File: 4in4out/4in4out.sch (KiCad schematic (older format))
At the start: 60 parts

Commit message: Suppression des PNP
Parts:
- removed D? (x4): LED, symbol LED
- removed D? (x3): DIODE, symbol DIODE
- removed K? (x3): G5T-1-12VDC, symbol G5T-1-12VDC
- removed P? (x3): CONN_2, symbol CONN_2
- removed Q? (x4): PNP, symbol PNP
- removed Q? (x3): NPN, symbol NPN
- removed R? (x12): R, symbol R
- added D? (x4): LED, symbol LED
- added D? (x3): DIODE, symbol DIODE
- added K? (x3): G5T-1-12VDC, symbol G5T-1-12VDC
- added P? (x3): CONN_2, symbol CONN_2
- added Q? (x3): NPN, symbol NPN
- added R? (x8): R, symbol R
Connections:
- wire segments 125 -> 113
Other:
- moved on the sheet: D?, K?, P?, Q?

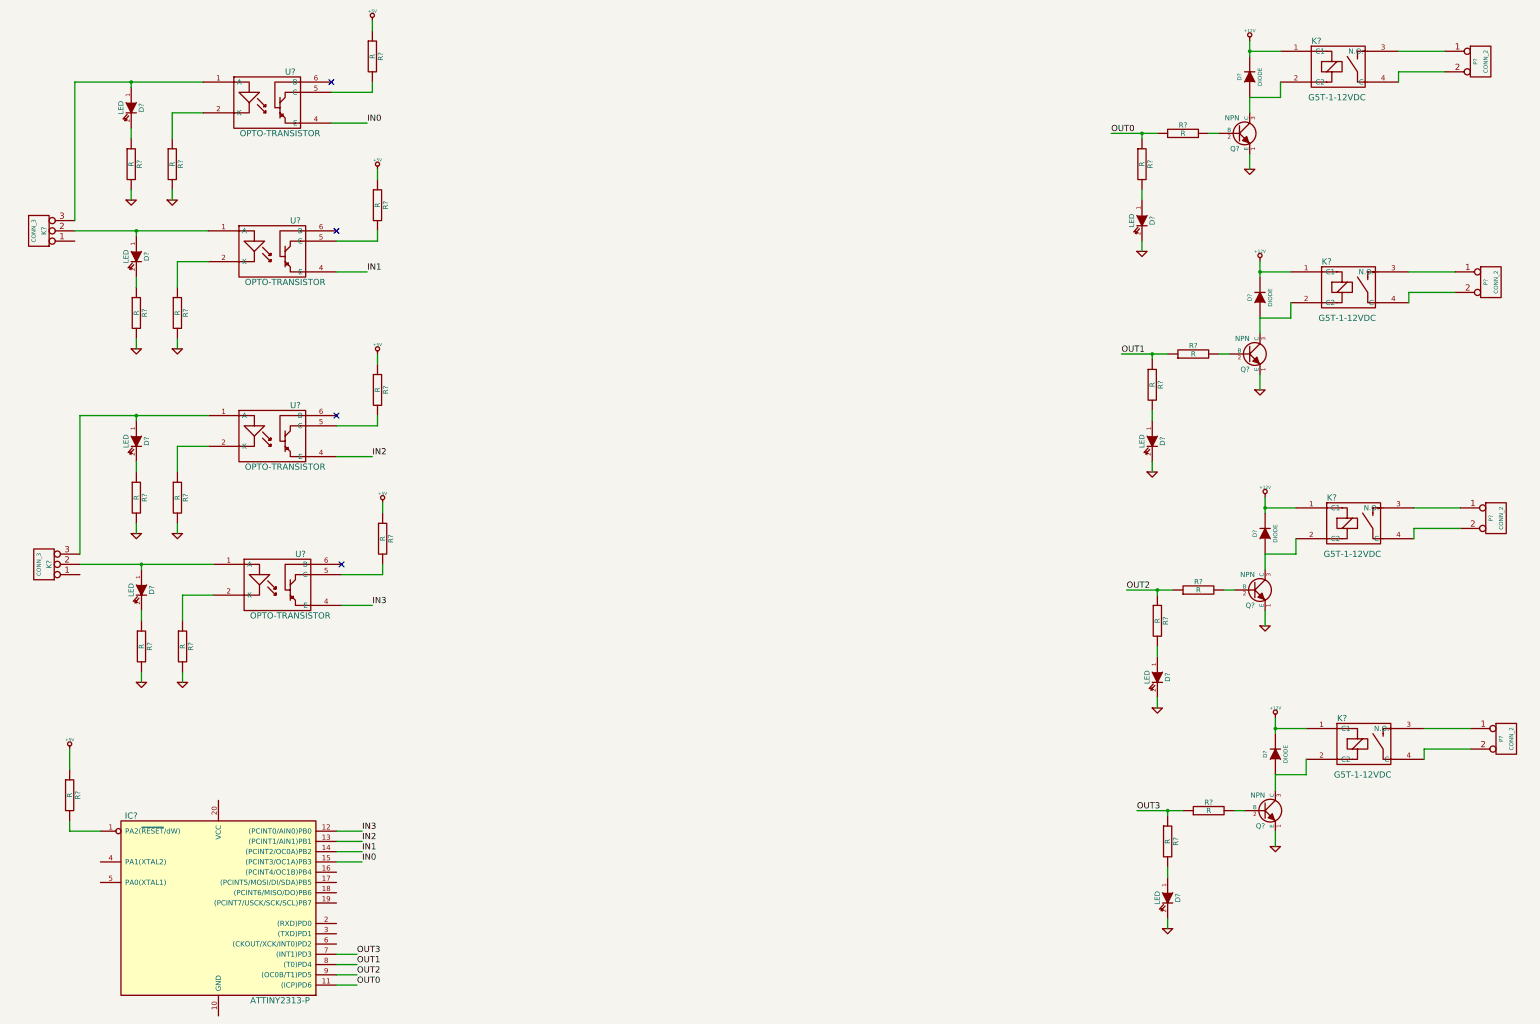
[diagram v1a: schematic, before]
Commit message: Mise ? jour de la carte 4in4out : Ajout des connecteurs et nommage des composants
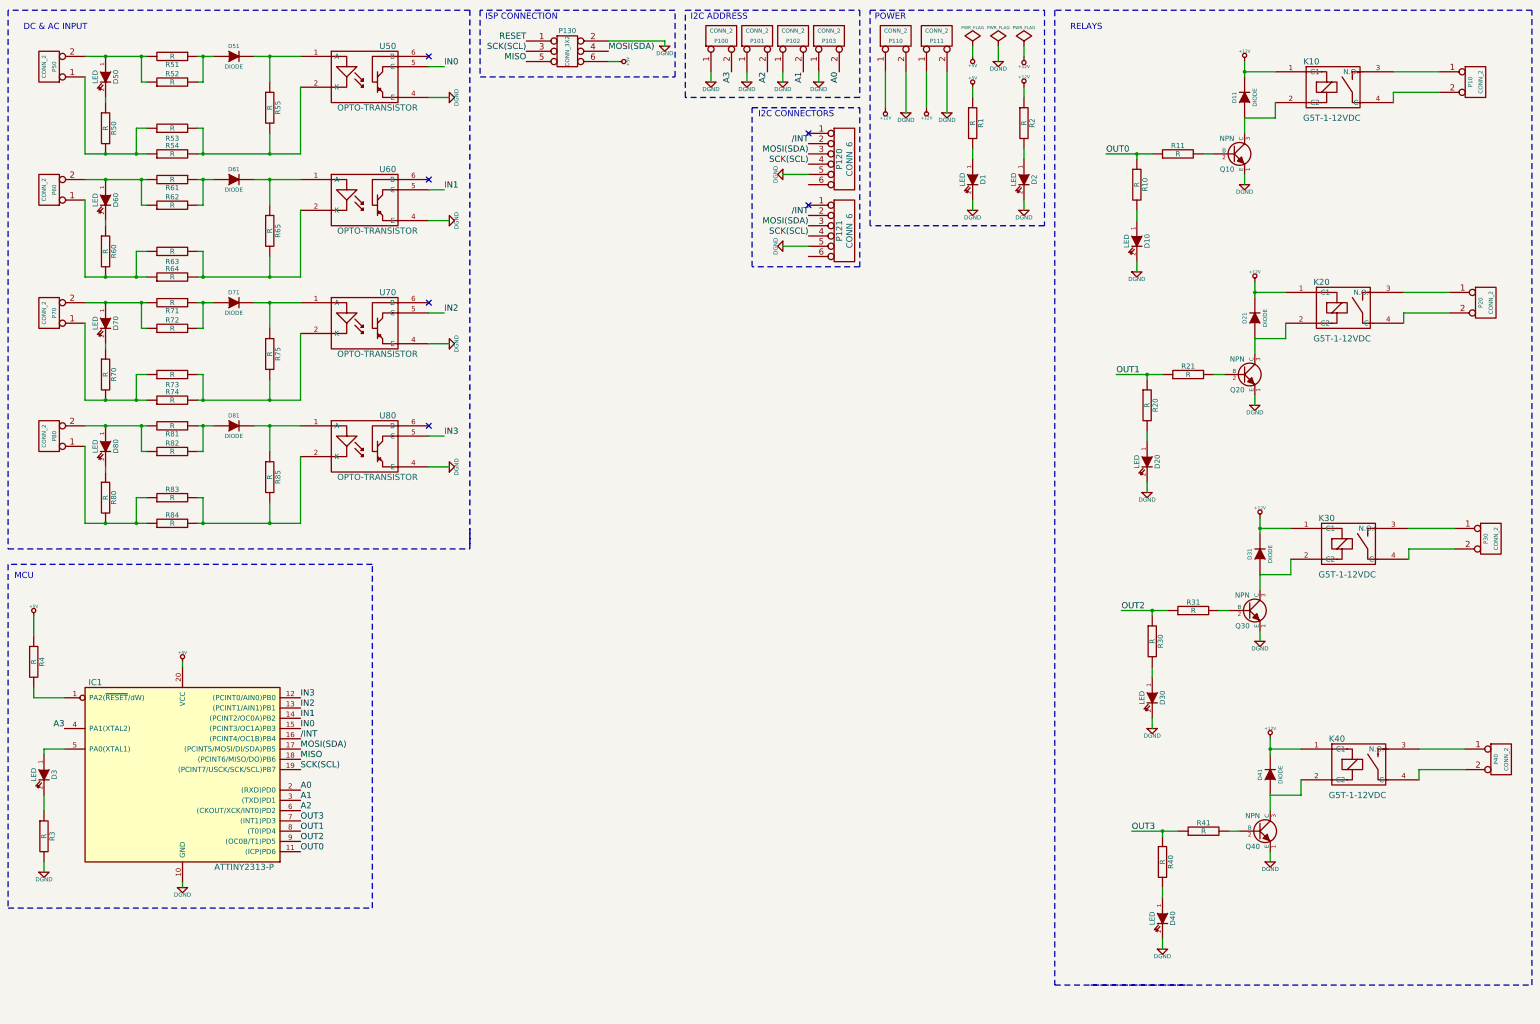
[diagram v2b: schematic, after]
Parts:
- removed D? (x4): LED, symbol LED
- removed K? (x2): CONN_3, symbol CONN_3
- removed R? (x12): R, symbol R
- removed U? (x3): OPTO-TRANSISTOR, symbol OPTO-TRANSISTOR
- added D1, D2, D3, D50, D60, D70, D80: LED, symbol LED
- added D51, D61, D71, D81: DIODE, symbol DIODE
- added P100, P101, P102, P103, P110, P111, P50, P60, P70, P80: CONN_2, symbol CONN_2
- added P120, P121: CONN_6, symbol CONN_6
- added P130: CONN_3X2, symbol CONN_3X2
- added R1, R2, R3, R50, R51, R52, R53, R54, R55, R60, R61, R62, R63, R64, R65, R70, R71, R72, R73, R74, R75, R80, R81, R82, R83, R84, R85: R, symbol R
- added U60, U70, U80: OPTO-TRANSISTOR, symbol OPTO-TRANSISTOR
- gave numbers to parts that had none: 31
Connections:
- net GND is gone; now on net DGND: D10.2 (K), D20.2 (K), D30.2 (K), D40.2 (K), Q10.1 (E), Q20.1 (E), Q30.1 (E), Q40.1 (E)
- net +12V: now also P110.1 (P1), P111.1 (P1), R2.1
- net +5V: now also IC1.20 (VCC), P130.6, R1.1
- net IN0: now also U50.5 (C); no longer U50.4 (E)
- net IN1: now also U60.5 (C)
- net IN2: now also U70.5 (C)
- net IN3: now also U80.5 (C)
- net DGND: now reaches IC1.10 (GND)
- net DGND: now also U50.4 (E), D1.2 (K), D2.2 (K), P100.1 (P1), P101.1 (P1), P102.1 (P1), P103.1 (P1), P110.2 (PM), P111.2 (PM), P120.5, P121.5, P130.2, R3.2, U60.4 (E), U70.4 (E), U80.4 (E)
- net /INT: now reaches IC1.16 ((PCINT4/OC1B)PB4)
- net /INT: now also P120.2, P121.2
- net MOSI(SDA): now reaches IC1.17 ((PCINT5/MOSI/DI/SDA)PB5)
- net MOSI(SDA): now also P120.3, P121.3, P130.4
- net MISO: now reaches IC1.18 ((PCINT6/MISO/DO)PB6)
- net MISO: now also P130.5
- net SCK(SCL): now reaches IC1.19 ((PCINT7/USCK/SCK/SCL)PB7)
- net SCK(SCL): now also P120.4, P121.4, P130.3
- net A0: now reaches IC1.2 ((RXD)PD0)
- net A0: now also P103.2 (PM)
- net A1: now reaches IC1.3 ((TXD)PD1)
- net A1: now also P102.2 (PM)
- net A3: now reaches IC1.4 (PA1(XTAL2))
- net A3: now also P100.2 (PM)
- net at IC1.5 (PA0(XTAL1)): now also D3.1 (A)
- net A2: now reaches IC1.6 ((CKOUT/XCK/INT0)PD2)
- net A2: now also P101.2 (PM)
- net at U50.1 (A): now also D51.2 (K), R55.1
- net at U50.2 (K): now also R53.2, R54.2, R55.2
- new net: D51.1 (A), R51.1, R52.2
- new net: D50.1 (A), P50.2 (PM), R51.2, R52.1
- new net: P50.1 (P1), R50.2, R53.1, R54.1
- new net: D50.2 (K), R50.1
- new net: D61.2 (K), R65.1, U60.1 (A)
- new net: R63.2, R64.2, R65.2, U60.2 (K)
- new net: D61.1 (A), R61.1, R62.2
- new net: D60.1 (A), P60.2 (PM), R61.2, R62.1
- new net: P60.1 (P1), R60.2, R63.1, R64.1
- new net: D60.2 (K), R60.1
- new net: D71.2 (K), R75.1, U70.1 (A)
- new net: R73.2, R74.2, R75.2, U70.2 (K)
- new net: D71.1 (A), R71.1, R72.2
- new net: D70.1 (A), P70.2 (PM), R71.2, R72.1
- new net: P70.1 (P1), R70.2, R73.1, R74.1
- new net: D70.2 (K), R70.1
- new net: D81.2 (K), R85.1, U80.1 (A)
- new net: R83.2, R84.2, R85.2, U80.2 (K)
- new net: D81.1 (A), R81.1, R82.2
- new net: D80.1 (A), P80.2 (PM), R81.2, R82.1
- new net: P80.1 (P1), R80.2, R83.1, R84.1
- new net: D80.2 (K), R80.1
- new net: D3.2 (K), R3.1
- new net: D2.1 (A), R2.2
- new net: D1.1 (A), R1.2
- new net RESET: P130.1
- no-connect marks 4 -> 6
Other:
- note added: "DC & AC INPUT"
- note added: "I2C ADDRESS"
- note added: "I2C CONNECTORS"
- note added: "ISP CONNECTION"
- note added: "MCU"
- note added: "POWER"
- note added: "RELAYS"
- moved on the sheet: D10, D11, D20, D21, D30, D31, D40, D41, IC1, K10, K20, K30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

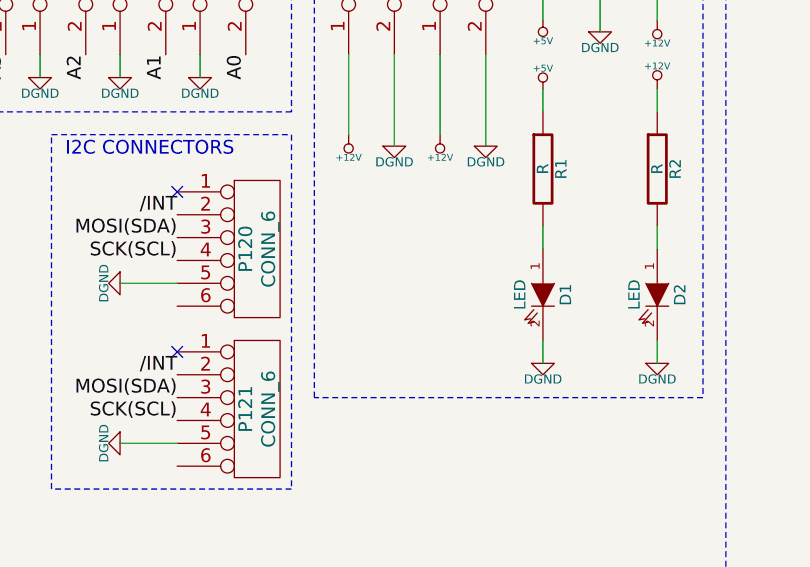
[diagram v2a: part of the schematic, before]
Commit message: Ajout de capa pour le 5V dans le sch?ma, association des composants avec leur module, cr?ation du module G5T-1-12VDC (Pin a revoir)
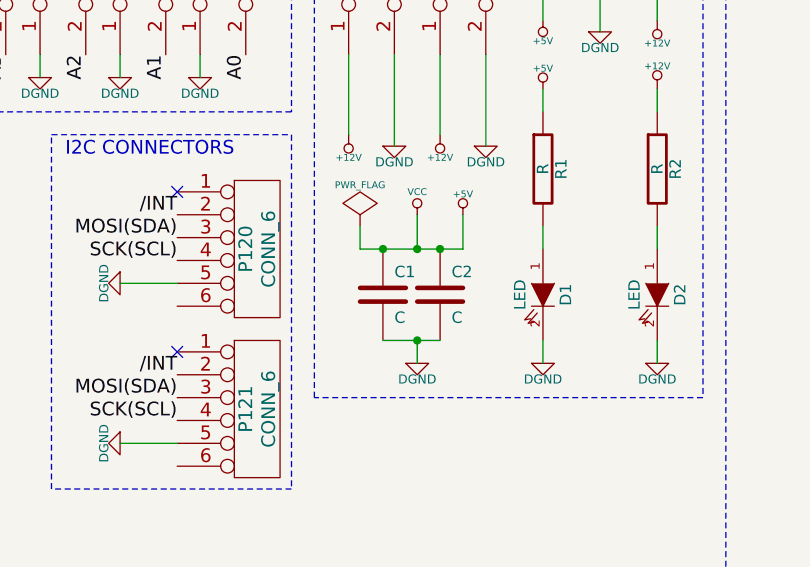
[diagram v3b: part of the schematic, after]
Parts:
- added C1, C2: C, symbol C
- K10: footprint (none) -> G5T-1-12VDC
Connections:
- net +5V: now also C1.1, C2.1
- net DGND: now also C1.2, C2.2
